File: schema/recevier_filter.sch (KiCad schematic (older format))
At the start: 0 parts

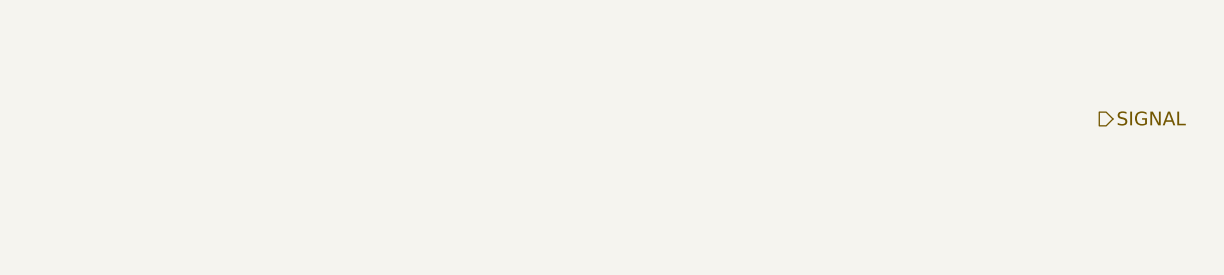
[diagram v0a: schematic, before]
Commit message: Preamp prototype, add IR LED and photodiode
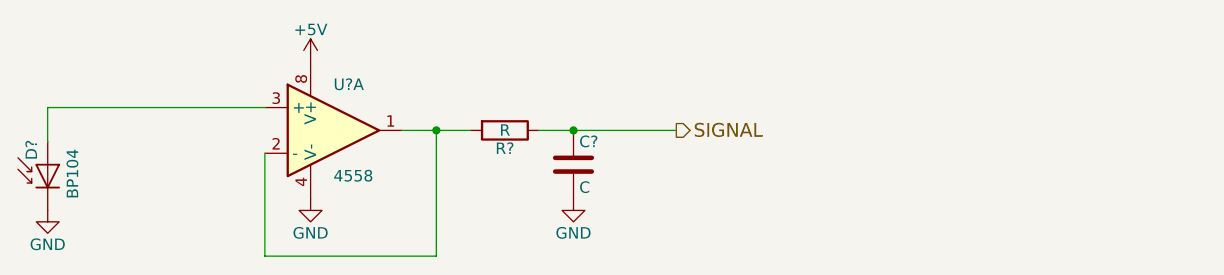
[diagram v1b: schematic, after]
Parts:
- added C?: C, symbol C
- added D?: BP104, symbol D_Photo
- added R?: R, symbol R
- added U?: 4558, symbol 4558
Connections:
- net SIGNAL: now also C?.1, R?.1
- new net: D?.2 (A), U?.3 (+)
- new net: R?.2, U?.1, U?.2 (-)
- new net +5V: U?.8 (V+)
- new net GND: C?.2, D?.1 (K), U?.4 (V-)
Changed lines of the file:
@@
 $Descr A4 11693 8268
 encoding utf-8
-Sheet 5 6
+Sheet 4 6
 Title ""
 Date ""
@@
 Comment4 ""
 $EndDescr
-Text HLabel 8900 3300 2    60   Output ~ 0
+Text HLabel 7050 3350 2    60   Output ~ 0
 SIGNAL
+$Comp
+L D_Photo D?
+U 1 1 5910653E
+P 4300 3500
+F 0 "D?" H 4320 3570 50  0000 L CNN
+F 1 "BP104" H 4260 3390 50  0000 C CNN
+F 2 "" H 4250 3500 50  0000 C CNN
+F 3 "" H 4250 3500 50  0000 C CNN
+	1    4300 3500
+	0    -1   -1   0
+$EndComp
+$Comp
+L GND #PWR?
+U 1 1 59106585
+P 4300 3700
+F 0 "#PWR?" H 4300 3450 50  0001 C CNN
+F 1 "GND" H 4300 3550 50  0000 C CNN
+F 2 "" H 4300 3700 50  0000 C CNN
+F 3 "" H 4300 3700 50  0000 C CNN
+	1    4300 3700
+	1    0    0    -1
+$EndComp
+$Comp
+L 4558 U?
+U 1 1 591066A9
+P 5550 3350
+F 0 "U?" H 5550 3550 50  0000 L CNN
+F 1 "4558" H 5550 3150 50  0000 L CNN
+F 2 "" H 5550 3350 50  0000 C CNN
+F 3 "" H 5550 3350 50  0000 C CNN
+	1    5550 3350
+	1    0    0    -1
+$EndComp
+$Comp
+L R R?
+U 1 1 591066D0
+P 6300 3350
+F 0 "R?" V 6380 3350 50  0000 C CNN
+F 1 "R" V 6300 3350 50  0000 C CNN
+F 2 "" V 6230 3350 50  0000 C CNN
+F 3 "" H 6300 3350 50  0000 C CNN
+	1    6300 3350
+	0    1    1    0
+$EndComp
+$Comp
+L GND #PWR?
+U 1 1 591066FE
+P 5450 3650
+F 0 "#PWR?" H 5450 3400 50  0001 C CNN
+F 1 "GND" H 5450 3500 50  0000 C CNN
+F 2 "" H 5450 3650 50  0000 C CNN
+F 3 "" H 5450 3650 50  0000 C CNN
+	1    5450 3650
+	1    0    0    -1
+$EndComp
+$Comp
+L C C?
+U 1 1 5910676C
+P 6600 3500
+F 0 "C?" H 6625 3600 50  0000 L CNN
+F 1 "C" H 6625 3400 50  0000 L CNN
+F 2 "" H 6638 3350 50  0000 C CNN
+F 3 "" H 6600 3500 50  0000 C CNN
+	1    6600 3500
+	1    0    0    -1
+$EndComp
+$Comp
+L GND #PWR?
+U 1 1 59106802
+P 6600 3650
+F 0 "#PWR?" H 6600 3400 50  0001 C CNN
+F 1 "GND" H 6600 3500 50  0000 C CNN
+F 2 "" H 6600 3650 50  0000 C CNN
+F 3 "" H 6600 3650 50  0000 C CNN
+	1    6600 3650
+	1    0    0    -1
+$EndComp
+Wire Wire Line
+	4300 3400 4300 3250
+Wire Wire Line
+	4300 3250 5250 3250
+Wire Wire Line
+	6000 3350 6000 3900
+Wire Wire Line
+	6000 3900 5250 3900
+Wire Wire Line
+	5250 3900 5250 3450
+Wire Wire Line
+	5850 3350 6150 3350
+Wire Wire Line
+	6450 3350 6600 3350
+Wire Wire Line
+	6600 3350 7050 3350
+Connection ~ 6600 3350
+$Comp
+L +5V #PWR?
+U 1 1 5910696F
+P 5450 3050
+F 0 "#PWR?" H 5450 2900 50  0001 C CNN
+F 1 "+5V" H 5450 3190 50  0000 C CNN
+F 2 "" H 5450 3050 50  0000 C CNN
+F 3 "" H 5450 3050 50  0000 C CNN
+	1    5450 3050
+	1    0    0    -1
+$EndComp
+Connection ~ 6000 3350
 $EndSCHEMATC

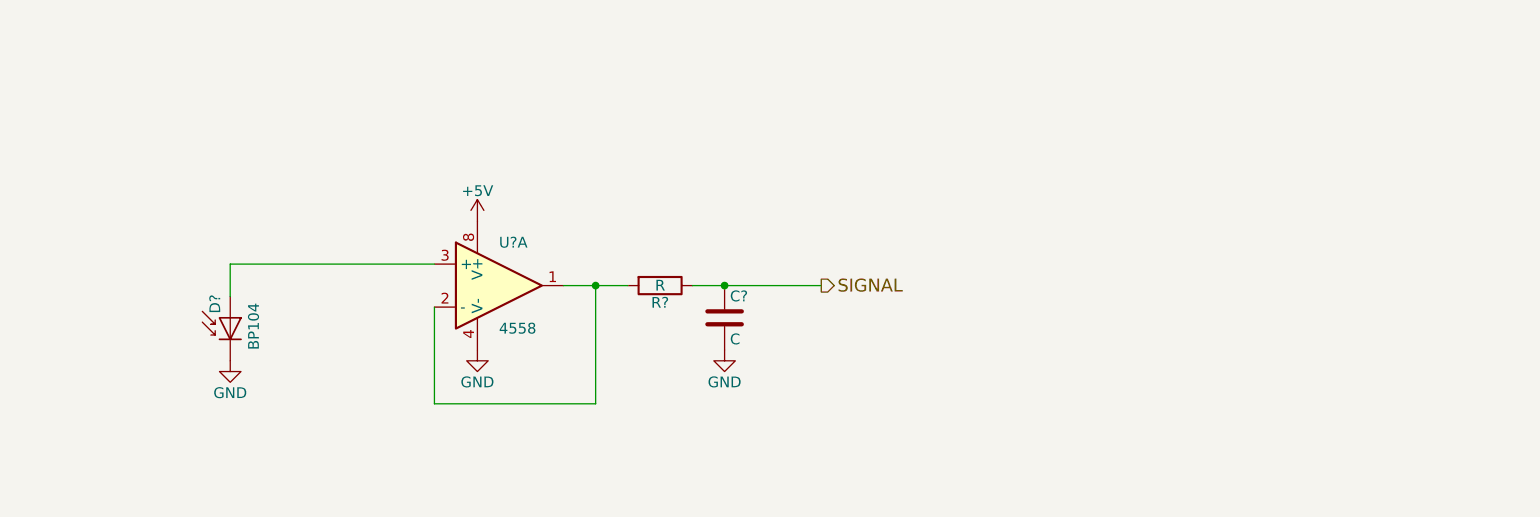
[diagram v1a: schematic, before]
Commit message: Preamp & filter proposal
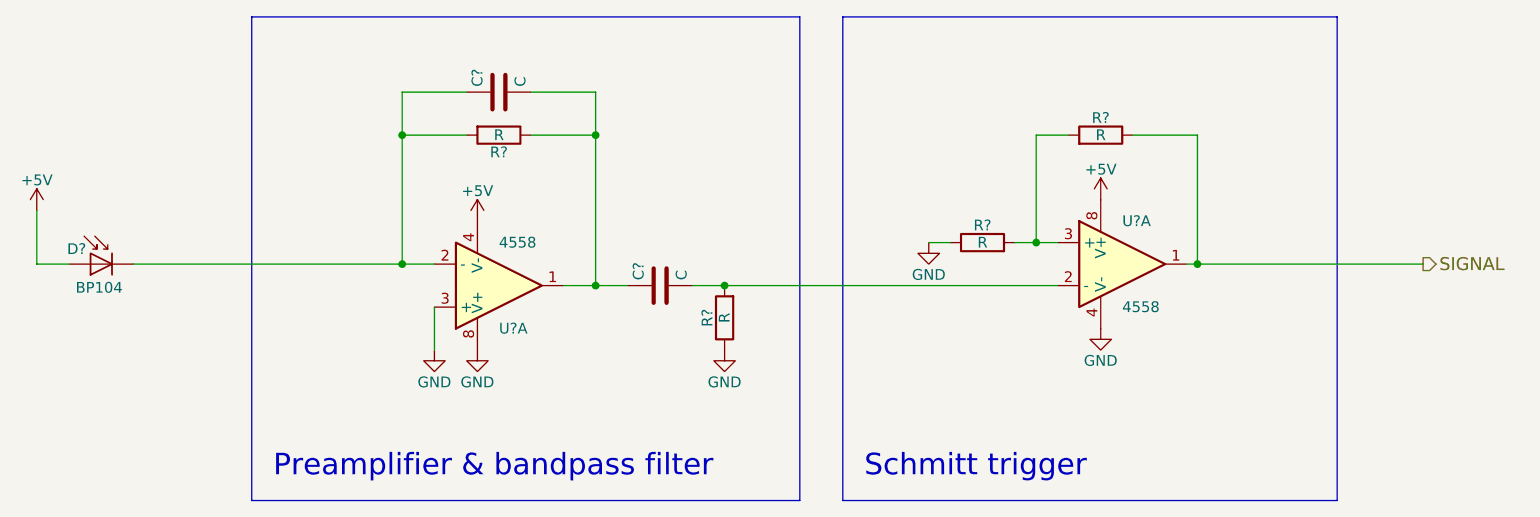
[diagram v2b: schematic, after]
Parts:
- added C?: C, symbol C
- added R? (x3): R, symbol R
- added U?: 4558, symbol 4558
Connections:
- net +5V: now also D?.2 (A), U?.4 (V-), U?.8 (V+); no longer U?.8 (V+)
- net GND: now also R?.1, U?.3 (+), U?.8 (V+), R?.1, U?.4 (V-); no longer C?.2, D?.1 (K), U?.4 (V-)
- net SIGNAL: now also R?.1, U?.1; no longer C?.1, R?.1
- new net: C?.1, D?.1 (K), R?.2, U?.2 (-)
- new net: C?.1, C?.2, R?.1, U?.1
- new net: C?.2, R?.2, U?.2 (-)
- new net: R?.2, R?.2, U?.3 (+)
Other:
- note added: "Preamplifier & bandpass filter"
- note added: "Schmitt trigger"
- moved on the sheet: C?, D?, R?
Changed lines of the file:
@@
 Comment4 ""
 $EndDescr
-Text HLabel 7050 3350 2    60   Output ~ 0
+Text HLabel 9850 3250 2    60   Output ~ 0
 SIGNAL
 $Comp
 L D_Photo D?
 U 1 1 5910653E
-P 4300 3500
-F 0 "D?" H 4320 3570 50  0000 L CNN
-F 1 "BP104" H 4260 3390 50  0000 C CNN
-F 2 "" H 4250 3500 50  0000 C CNN
-F 3 "" H 4250 3500 50  0000 C CNN
-	1    4300 3500
-	0    -1   -1   0
-$EndComp
-$Comp
-L GND #PWR?
-U 1 1 59106585
-P 4300 3700
-F 0 "#PWR?" H 4300 3450 50  0001 C CNN
-F 1 "GND" H 4300 3550 50  0000 C CNN
-F 2 "" H 4300 3700 50  0000 C CNN
-F 3 "" H 4300 3700 50  0000 C CNN
-	1    4300 3700
-	1    0    0    -1
+P 3650 3250
+F 0 "D?" H 3670 3320 50  0000 L CNN
+F 1 "BP104" H 3610 3140 50  0000 C CNN
+F 2 "" H 3600 3250 50  0000 C CNN
+F 3 "" H 3600 3250 50  0000 C CNN
+	1    3650 3250
+	-1   0    0    -1
 $EndComp
 $Comp
@@
 F 3 "" H 5550 3350 50  0000 C CNN
 	1    5550 3350
-	1    0    0    -1
+	1    0    0    1
 $EndComp
 $Comp
 L R R?
 U 1 1 591066D0
-P 6300 3350
-F 0 "R?" V 6380 3350 50  0000 C CNN
-F 1 "R" V 6300 3350 50  0000 C CNN
-F 2 "" V 6230 3350 50  0000 C CNN
-F 3 "" H 6300 3350 50  0000 C CNN
-	1    6300 3350
-	0    1    1    0
+P 6600 3500
+F 0 "R?" V 6680 3500 50  0000 C CNN
+F 1 "R" V 6600 3500 50  0000 C CNN
+F 2 "" V 6530 3500 50  0000 C CNN
+F 3 "" H 6600 3500 50  0000 C CNN
+	1    6600 3500
+	-1   0    0    1
 $EndComp
 $Comp
@@
 L C C?
 U 1 1 5910676C
-P 6600 3500
-F 0 "C?" H 6625 3600 50  0000 L CNN
-F 1 "C" H 6625 3400 50  0000 L CNN
-F 2 "" H 6638 3350 50  0000 C CNN
-F 3 "" H 6600 3500 50  0000 C CNN
-	1    6600 3500
-	1    0    0    -1
+P 6300 3350
+F 0 "C?" H 6325 3450 50  0000 L CNN
+F 1 "C" H 6325 3250 50  0000 L CNN
+F 2 "" H 6338 3200 50  0000 C CNN
+F 3 "" H 6300 3350 50  0000 C CNN
+	1    6300 3350
+	0    -1   -1   0
 $EndComp
 $Comp
@@
 $EndComp
 Wire Wire Line
-	4300 3400 4300 3250
-Wire Wire Line
-	4300 3250 5250 3250
-Wire Wire Line
-	6000 3350 6000 3900
-Wire Wire Line
-	6000 3900 5250 3900
-Wire Wire Line
-	5250 3900 5250 3450
+	5250 3650 5250 3450
 Wire Wire Line
 	5850 3350 6150 3350
 Wire Wire Line
-	6450 3350 6600 3350
-Wire Wire Line
-	6600 3350 7050 3350
+	6450 3350 8150 3350
 Connection ~ 6600 3350
 $Comp
@@
 $EndComp
 Connection ~ 6000 3350
+$Comp
+L GND #PWR?
+U 1 1 59109B08
+P 5250 3650
+F 0 "#PWR?" H 5250 3400 50  0001 C CNN
+F 1 "GND" H 5250 3500 50  0000 C CNN
+F 2 "" H 5250 3650 50  0000 C CNN
+F 3 "" H 5250 3650 50  0000 C CNN
+	1    5250 3650
+	1    0    0    -1
+$EndComp
+Wire Wire Line
+	3850 3250 5250 3250
+Wire Wire Line
+	3400 3250 3400 3000
+$Comp
+L R R?
+U 1 1 59109F5B
+P 5550 2650
+F 0 "R?" V 5630 2650 50  0000 C CNN
+F 1 "R" V 5550 2650 50  0000 C CNN
+F 2 "" V 5480 2650 50  0000 C CNN
+F 3 "" H 5550 2650 50  0000 C CNN
+	1    5550 2650
+	0    1    1    0
+$EndComp
+$Comp
+L C C?
+U 1 1 59109F88
+P 5550 2450
+F 0 "C?" H 5575 2550 50  0000 L CNN
+F 1 "C" H 5575 2350 50  0000 L CNN
+F 2 "" H 5588 2300 50  0000 C CNN
+F 3 "" H 5550 2450 50  0000 C CNN
+	1    5550 2450
+	0    -1   -1   0
+$EndComp
+Wire Wire Line
+	5100 2450 5100 3250
+Wire Wire Line
+	5100 2450 5400 2450
+Connection ~ 5100 3250
+Wire Wire Line
+	5400 2650 5100 2650
+Connection ~ 5100 2650
+Wire Wire Line
+	5700 2450 6000 2450
+Wire Wire Line
+	6000 2450 6000 3350
+Wire Wire Line
+	5700 2650 6000 2650
+Connection ~ 6000 2650
+$Comp
+L +5V #PWR?
+U 1 1 5910A311
+P 3400 3000
+F 0 "#PWR?" H 3400 2850 50  0001 C CNN
+F 1 "+5V" H 3400 3140 50  0000 C CNN
+F 2 "" H 3400 3000 50  0000 C CNN
+F 3 "" H 3400 3000 50  0000 C CNN
+	1    3400 3000
+	1    0    0    -1
+$EndComp
+$Comp
+L 4558 U?
+U 1 1 5910A783
+P 8450 3250
+F 0 "U?" H 8450 3450 50  0000 L CNN
+F 1 "4558" H 8450 3050 50  0000 L CNN
+F 2 "" H 8450 3250 50  0000 C CNN
+F 3 "" H 8450 3250 50  0000 C CNN
+	1    8450 3250
+	1    0    0    -1
+$EndComp
+$Comp
+L R R?
+U 1 1 5910A9B3
+P 8350 2650
+F 0 "R?" V 8430 2650 50  0000 C CNN
+F 1 "R" V 8350 2650 50  0000 C CNN
+F 2 "" V 8280 2650 50  0000 C CNN
+F 3 "" H 8350 2650 50  0000 C CNN
+	1    8350 2650
+	0    1    -1   0
+$EndComp
+$Comp
+L R R?
+U 1 1 5910A9E7
+P 7800 3150
+F 0 "R?" V 7880 3150 50  0000 C CNN
+F 1 "R" V 7800 3150 50  0000 C CNN
+F 2 "" V 7730 3150 50  0000 C CNN
+F 3 "" H 7800 3150 50  0000 C CNN
+	1    7800 3150
+	0    -1   -1   0
+$EndComp
+Wire Wire Line
+	8750 3250 9850 3250
+Wire Wire Line
+	8200 2650 8050 2650
+Wire Wire Line
+	8050 2650 8050 3150
+Wire Wire Line
+	7950 3150 8150 3150
+Connection ~ 8050 3150
+Wire Wire Line
+	8500 2650 8800 2650
+Wire Wire Line
+	8800 2650 8800 3250
+Connection ~ 8800 3250
+$Comp
+L GND #PWR?
+U 1 1 5910AC6D
+P 7550 3150
+F 0 "#PWR?" H 7550 2900 50  0001 C CNN
+F 1 "GND" H 7550 3000 50  0000 C CNN
+F 2 "" H 7550 3150 50  0000 C CNN
+F 3 "" H 7550 3150 50  0000 C CNN
+	1    7550 3150
+	1    0    0    -1
+$EndComp
+Wire Wire Line
+	7550 3150 7650 3150
+$Comp
+L +5V #PWR?
+U 1 1 5910ADF1
+P 8350 2950
+F 0 "#PWR?" H 8350 2800 50  0001 C CNN
+F 1 "+5V" H 8350 3090 50  0000 C CNN
+F 2 "" H 8350 2950 50  0000 C CNN
+F 3 "" H 8350 2950 50  0000 C CNN
+	1    8350 2950
+	1    0    0    -1
+$EndComp
+$Comp
+L GND #PWR?
+U 1 1 5910B09A
+P 8350 3550
+F 0 "#PWR?" H 8350 3300 50  0001 C CNN
+F 1 "GND" H 8350 3400 50  0000 C CNN
+F 2 "" H 8350 3550 50  0000 C CNN
+F 3 "" H 8350 3550 50  0000 C CNN
+	1    8350 3550
+	1    0    0    -1
+$EndComp
+Wire Bus Line
+	7150 2100 7150 4350
+Wire Bus Line
+	7150 4350 9450 4350
+Wire Bus Line
+	9450 4350 9450 2100
+Wire Bus Line
+	9450 2100 7150 2100
+Wire Bus Line
+	6950 2100 6950 4350
+Wire Bus Line
+	6950 2100 4400 2100
+Wire Bus Line
+	4400 2100 4400 4350
+Wire Bus Line
+	4400 4350 6950 4350
+Wire Wire Line
+	3550 3250 3400 3250
+Text Notes 4500 4250 0    100  ~ 0
+Preamplifier & bandpass filter
+Text Notes 7250 4250 0    100  ~ 0
+Schmitt trigger
 $EndSCHEMATC
